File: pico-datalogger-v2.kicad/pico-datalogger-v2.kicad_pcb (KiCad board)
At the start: 2 copper layers, 46 x 60 mm, 35 parts, among them J1 JST-PH2 Bat, J10 Conn_PCB_2, J11 Conn_I2C1, J12 Conn_UART_5V, J13 Conn_I2C1, J14 Conn_I2C0, J2 Conn_Pico_Left, J3 Conn_Pico_Right, J4 Alt-Bat, J5 Conn_LoRa, J6 Conn_Display, J7 Conn_PCB_1, J8 Conn_ADC, J9 Conn_I2C0, Q1 AO3401A, Q2 AO3401A, SW1 SW_ON, SW2 SW_RUN, U1 74LVC2G74, U2 PCF8523T, U4 XTSD, Y1 Crystal

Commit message: added THT-connectors, finished routing
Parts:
- added J15: PCB_2_THT, Connector_PinHeader_2.54mm:PinHeader_1x08_P2.54mm_Vertical, F.Cu at (99.2, 119.7)
- added J16: LoRa_THT, Connector_PinHeader_2.54mm:PinHeader_1x08_P2.54mm_Vertical, F.Cu at (99.2, 147.4)
- added J17: Disp_THT, Connector_PinHeader_2.54mm:PinHeader_1x08_P2.54mm_Vertical, F.Cu at (137.1, 147.4)
- added R5: 10K, Resistor_SMD:R_0402_1005Metric, F.Cu at (128.3, 147.1)
- added R6: 100K, Resistor_SMD:R_0402_1005Metric, F.Cu at (128.4, 149.6)
- added R7: 10K, Resistor_SMD:R_0402_1005Metric, F.Cu at (123.1, 129.8)
- J4: value Alt-Bat -> PCB_1_THT; footprint Connector_PinHeader_2.54mm:PinHeader_1x02_P2.54mm_Vertical -> Connector_PinHeader_2.54mm:PinHeader_1x04_P2.54mm_Vertical; moved to F.Cu
- J7: footprint Connector_JST:JST_SUR_BM04B-SURS-TF_1x04-1MP_P0.80mm_Vertical -> Connector_JST:JST_SUR_BM08B-SURS-TF_1x08-1MP_P0.80mm_Vertical
- SW2: value SW_RUN -> SW_RST
- moved J4 36.5 mm to (108.2, 161.8), turned to 90 degrees
- moved J1 35.2 mm to (141.1, 110.8)
- moved J5 16.6 mm to (92.3, 156.2)
- moved J6 16.1 mm to (142.9, 156.2)
- moved H3 14.1 mm to (93.0, 167.0)
- moved SW1 11.3 mm to (127.5, 165.8)
- moved J7 11.3 mm to (112.0, 167.8)
- moved SW2 11.3 mm to (119.4, 165.8)
- moved H1 10.0 mm to (93.0, 103.0)
- moved H4 10.0 mm to (143.0, 167.0)
- moved J10 10.0 mm to (92.3, 131.5)
- moved J12 10.0 mm to (94.3, 120.9)
- moved BT1 3.60 mm to (136.8, 129.6)
- moved R2 0.85 mm to (122.0, 119.0), turned to -90 degrees
- moved C3 0.25 mm to (121.0, 143.4)
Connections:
- J4 pad 1: +BATT -> GND
- J4 pad 2: GND -> +3V3
- J7 pad 2: +3V3 -> GND
- J7 pad 3: /RUN -> +3V3
- J7 pad 4: /~{ON} -> +3V3
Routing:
- net +3V3: track 134.1 -> 223.5 mm
- net +BATT: track 66.7 -> 32.1 mm
- net /Display_CS: track 4.05 -> 32.5 mm, vias 0 -> 1
- net /SCLK0: track 23.1 -> 47.0 mm
- net /Lora_CS: track 7.16 -> 27.6 mm
- net /Lora_RST: track 7.88 -> 27.7 mm
- net /MISO1: track 16.9 -> 36.3 mm, vias 1 -> 0
- net /Display_RST: track 15.9 -> 35.3 mm, vias 0 -> 1
- net /MOSI1: track 8.60 -> 27.7 mm
- net /Display_DC: track 11.2 -> 30.1 mm
- net /SCLK1: track 10.3 -> 28.4 mm
- net /SDA: track 61.0 -> 79.1 mm
- net /MOSI0: track 27.0 -> 43.5 mm, vias 0 -> 2
- net /RUN: track 47.8 -> 63.6 mm
- net /Display_BUSY: track 27.5 -> 40.6 mm, vias 0 -> 1
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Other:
- board size 46 x 60 mm -> 56 x 70 mm
- board text added: "CS"
- board text added: "RST"
- board text removed: "RUN"

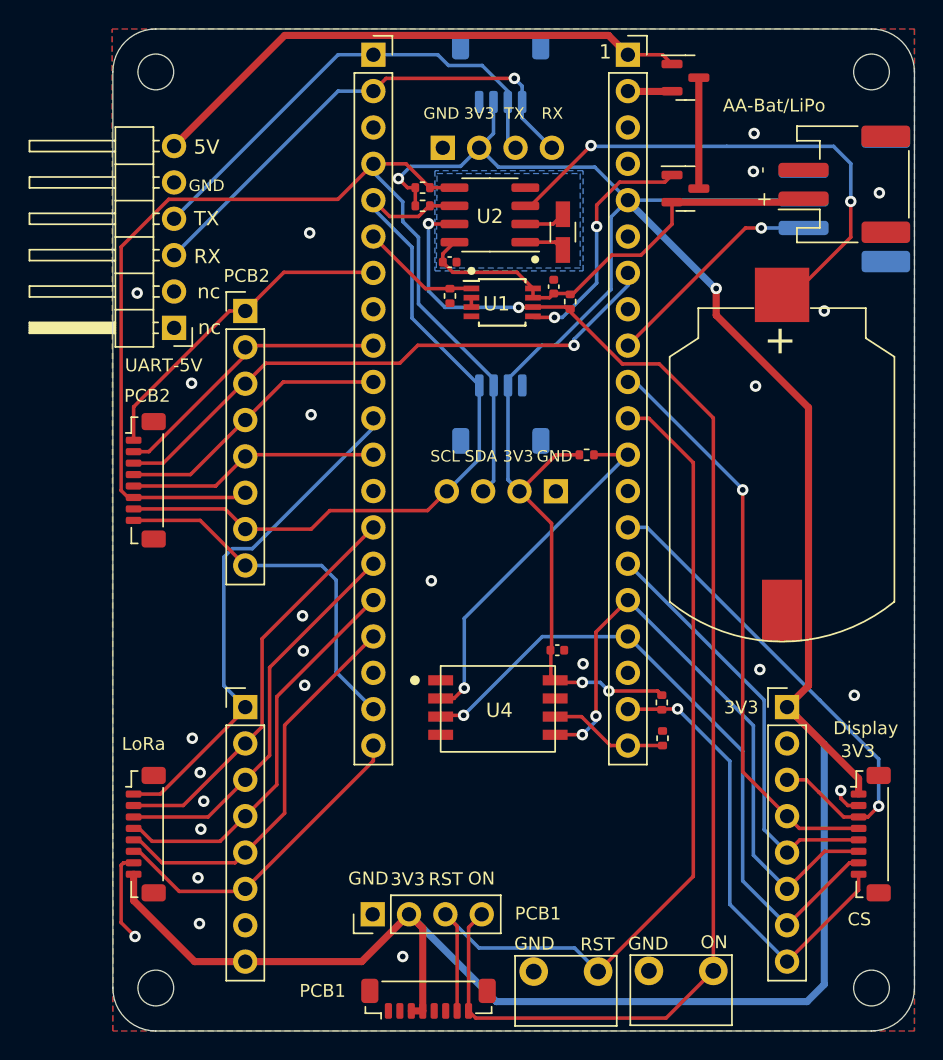
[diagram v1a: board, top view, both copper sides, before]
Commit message: Datalogger-v2 Rev 1.95: larger PCB-size, THT-connectors
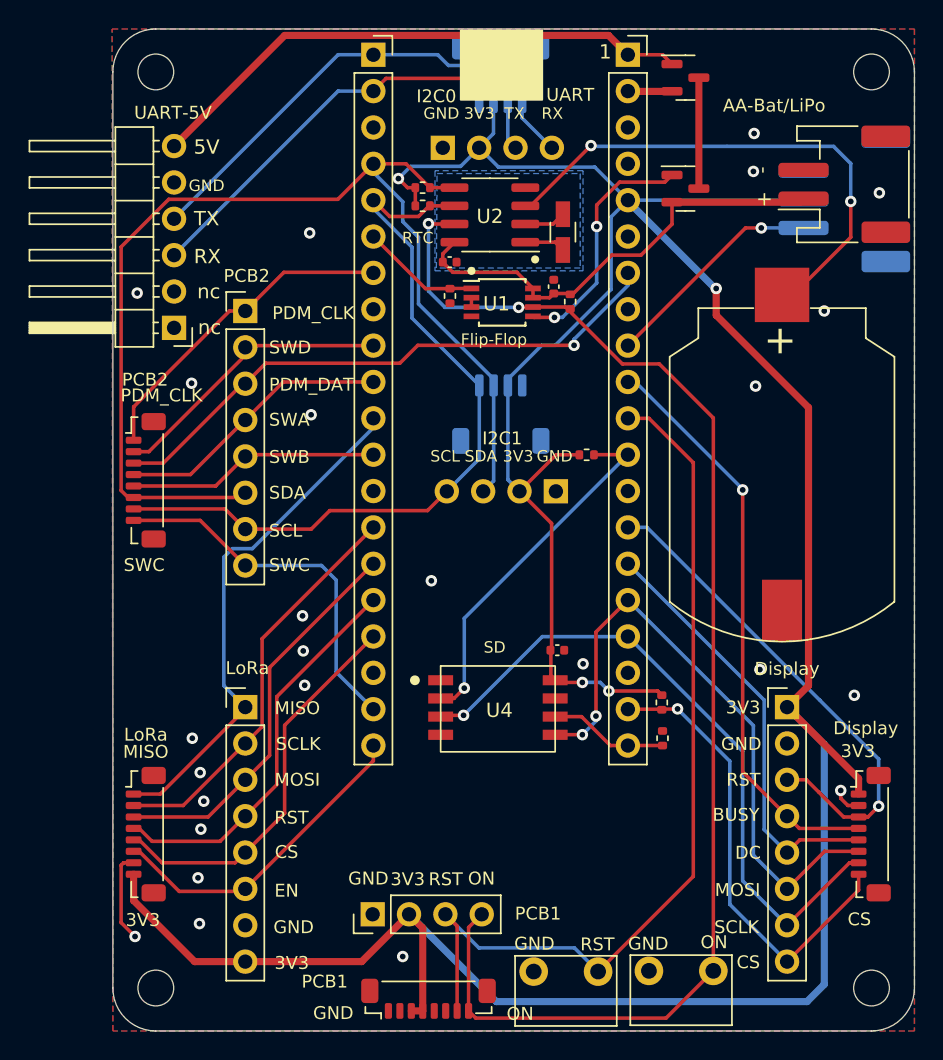
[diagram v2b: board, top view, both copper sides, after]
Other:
- board text added: "BUSY"
- board text added: "DC"
- board text added: "EN"
- board text added: "Flip-Flop"
- board text added: "I2C0"
- board text added: "MISO"
- board text added: "MOSI"
- board text added: "PDM_CLK"
- board text added: "PDM_DAT"
- board text added: "RTC"
- board text added: "SCLK"
- board text added: "SD"
- board text added: "SWA"
- board text added: "SWB"
- board text added: "SWC"
- board text added: "SWD"
- board text added: "UART"
- board text added: "https://github.com/bablokb/pcb-pico-datalogger https://opendeved.net/ilce Rev 1.95"
- board text removed: "https://github.com/bablokb/pcb-pico-datalogger https://opendeved.net/ilce Rev 0.94"

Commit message: Datalogger-v2 Rev 2.00: larger PCB-size, THT-connectors (ready for prod)
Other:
- board text added: "https://github.com/bablokb/pcb-pico-datalogger https://opendeved.net/ilce Rev 2.00"
- board text removed: "https://github.com/bablokb/pcb-pico-datalogger https://opendeved.net/ilce Rev 1.95"
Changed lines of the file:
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@@
     (property "Sheetname" "")
     (property "exclude_from_bom" "")
-    (attr through_hole exclude_from_bom)
+    (attr through_hole exclude_from_pos_files exclude_from_bom)
     (fp_text reference "J4" (at 0 -2.33 90) (layer "F.SilkS") hide
       (effects (font (size 1 1) (thickness 0.15)))
@@
     (property "Sheetname" "")
     (property "exclude_from_bom" "")
-    (attr through_hole exclude_from_bom)
+    (attr through_hole exclude_from_pos_files exclude_from_bom)
     (fp_text reference "J16" (at 0 -2.33) (layer "F.SilkS") hide
       (effects (font (size 1 1) (thickness 0.15)))
@@
     (property "Sheetname" "")
     (property "exclude_from_bom" "")
-    (attr through_hole exclude_from_bom)
+    (attr through_hole exclude_from_pos_files exclude_from_bom)
     (fp_text reference "J15" (at 0 -2.33) (layer "F.SilkS") hide
       (effects (font (size 1 1) (thickness 0.15)))
@@
     (pad "8" smd roundrect (at 2.8 0.85) (size 0.5 1.1) (layers "F.Cu" "F.Paste" "F.Mask") (roundrect_rratio 0.25)
       (net 39 "/~{ON}") (pinfunction "Pin_8") (pintype "passive"))
-    (pad "MP" smd roundrect (at -4.1 -0.55) (size 1.2 1.7) (layers "F.Cu" "F.Paste" "F.Mask") (roundrect_rratio 0.208333))
-    (pad "MP" smd roundrect (at 4.1 -0.55) (size 1.2 1.7) (layers "F.Cu" "F.Paste" "F.Mask") (roundrect_rratio 0.208333))
+    (pad "MP" smd roundrect (at -4.1 -0.55) (size 1.2 1.7) (layers "F.Cu" "F.Paste" "F.Mask") (roundrect_rratio 0.2083333333))
+    (pad "MP" smd roundrect (at 4.1 -0.55) (size 1.2 1.7) (layers "F.Cu" "F.Paste" "F.Mask") (roundrect_rratio 0.2083333333))
     (model "${KICAD6_3DMODEL_DIR}/Connector_JST.3dshapes/JST_SUR_BM08B-SURS-TF_1x08-1MP_P0.80mm_Vertical.wrl"
       (offset (xyz 0 0 0))
@@
     (property "Sheetname" "")
     (property "exclude_from_bom" "")
-    (attr through_hole exclude_from_bom)
+    (attr through_hole exclude_from_pos_files exclude_from_bom)
     (fp_text reference "J17" (at 0 -2.33) (layer "F.SilkS") hide
       (effects (font (size 1 1) (thickness 0.15)))
@@
     (property "Sheetfile" "pico-datalogger-v2.kicad_sch")
     (property "Sheetname" "")
-    (attr through_hole exclude_from_pos_files)
+    (property "exclude_from_bom" "")
+    (attr through_hole exclude_from_pos_files exclude_from_bom)
     (fp_text reference "SW1" (at -1.4 -3.6 90) (layer "F.SilkS") hide
       (effects (font (size 1 1) (thickness 0.15)))
@@
     (property "Sheetfile" "pico-datalogger-v2.kicad_sch")
     (property "Sheetname" "")
-    (attr through_hole exclude_from_pos_files)
+    (property "exclude_from_bom" "")
+    (attr through_hole exclude_from_pos_files exclude_from_bom)
     (fp_text reference "SW2" (at -1.25 -2.5 90) (layer "F.SilkS") hide
       (effects (font (size 1 1) (thickness 0.15)))
@@
     (effects (font (size 0.9 0.9) (thickness 0.15)) (justify mirror))
   )
-  (gr_text "https://github.com/bablokb/pcb-pico-datalogger\nhttps://opendeved.net/ilce               Rev 1.95" (at 93.35 123.75 90) (layer "B.SilkS")
+  (gr_text "https://github.com/bablokb/pcb-pico-datalogger\nhttps://opendeved.net/ilce               Rev 2.00" (at 93.35 123.75 90) (layer "B.SilkS")
     (effects (font (size 1 1) (thickness 0.15)) (justify left mirror))
   )

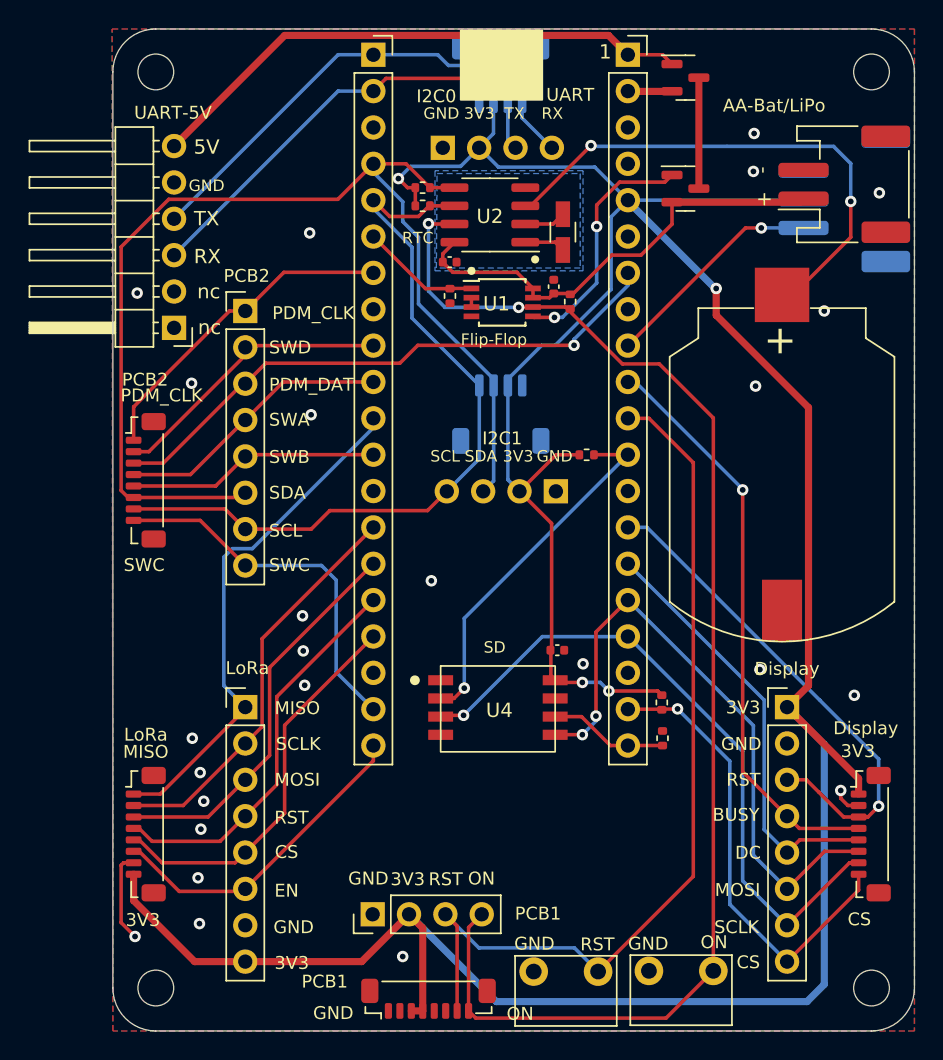
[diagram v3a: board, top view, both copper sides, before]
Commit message: Datalogger-v2 Rev 2.01: rotated display connector (ready for prod)
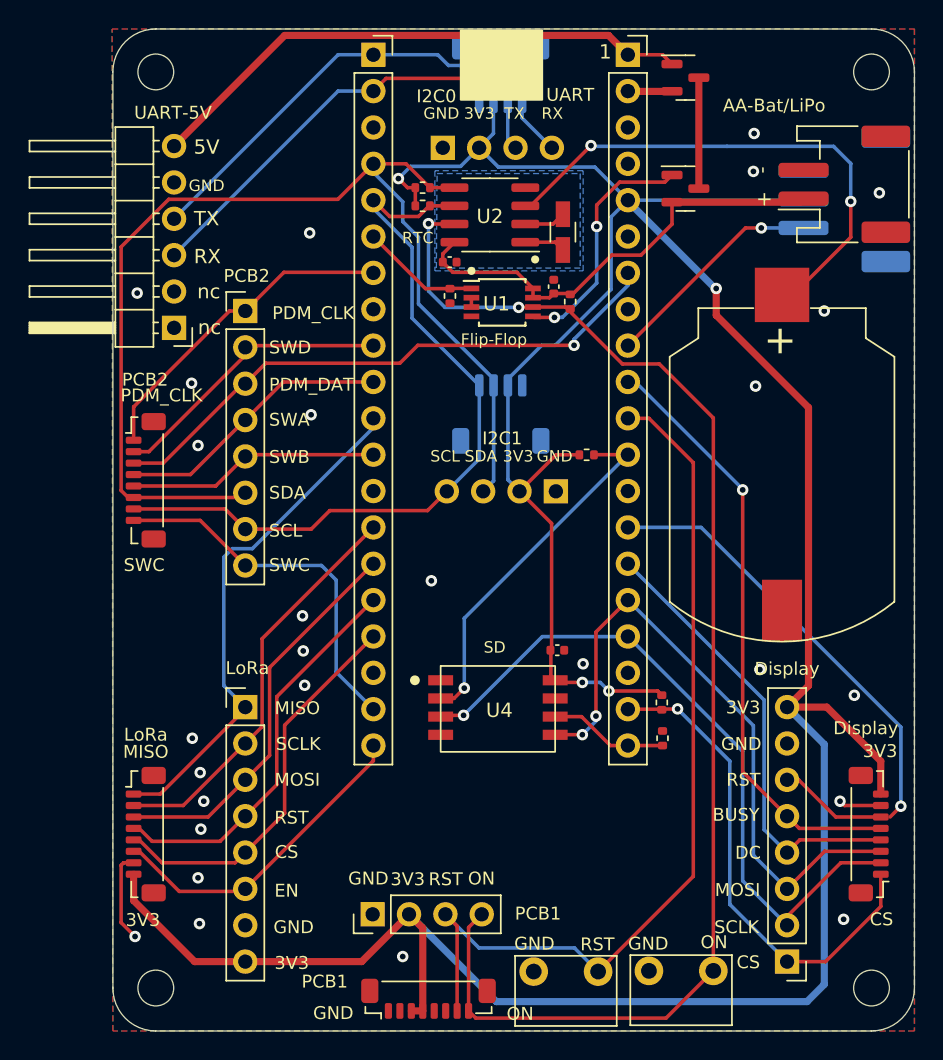
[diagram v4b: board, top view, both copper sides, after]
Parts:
- moved J17 17.8 mm to (137.1, 165.2), turned to 180 degrees
- moved J6 0.15 mm to (142.8, 156.2), turned to 90 degrees
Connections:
- J17 pad 1: +3V3 -> /Display_CS
- J17 pad 2: GND -> /SCLK0
- J17 pad 3: /Display_RST -> /MOSI0
- J17 pad 4: /Display_BUSY -> /Display_DC
- J17 pad 5: /Display_DC -> /Display_BUSY
- J17 pad 6: /MOSI0 -> /Display_RST
- J17 pad 7: /SCLK0 -> GND
- J17 pad 8: /Display_CS -> +3V3
- J6 pad 1: +3V3 -> /Display_CS
- J6 pad 2: GND -> /SCLK0
- J6 pad 3: /Display_RST -> /MOSI0
- J6 pad 4: /Display_BUSY -> /Display_DC
- J6 pad 5: /Display_DC -> /Display_BUSY
- J6 pad 6: /MOSI0 -> /Display_RST
- J6 pad 7: /SCLK0 -> GND
- J6 pad 8: /Display_CS -> +3V3
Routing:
- net /Display_RST: track 35.3 -> 39.1 mm
- net +3V3: track 223.5 -> 225.7 mm
- net /Display_CS: track 32.5 -> 34.7 mm
- net /SCLK0: track 47.0 -> 48.9 mm
- net /MOSI0: track 43.5 -> 45.0 mm
- net /Display_DC: track 30.1 -> 31.7 mm
- net /Display_BUSY: track 40.6 -> 42.2 mm
- net GND: track 8.33 -> 9.30 mm, vias 25 -> 27
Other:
- board text added: "https://github.com/bablokb/pcb-pico-datalogger https://opendeved.net/ilce Rev 2.01"
- board text removed: "https://github.com/bablokb/pcb-pico-datalogger https://opendeved.net/ilce Rev 2.00"

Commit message: Datalogger-v2 Rev 2.10: Stemma/Qt on top (ready for prod)
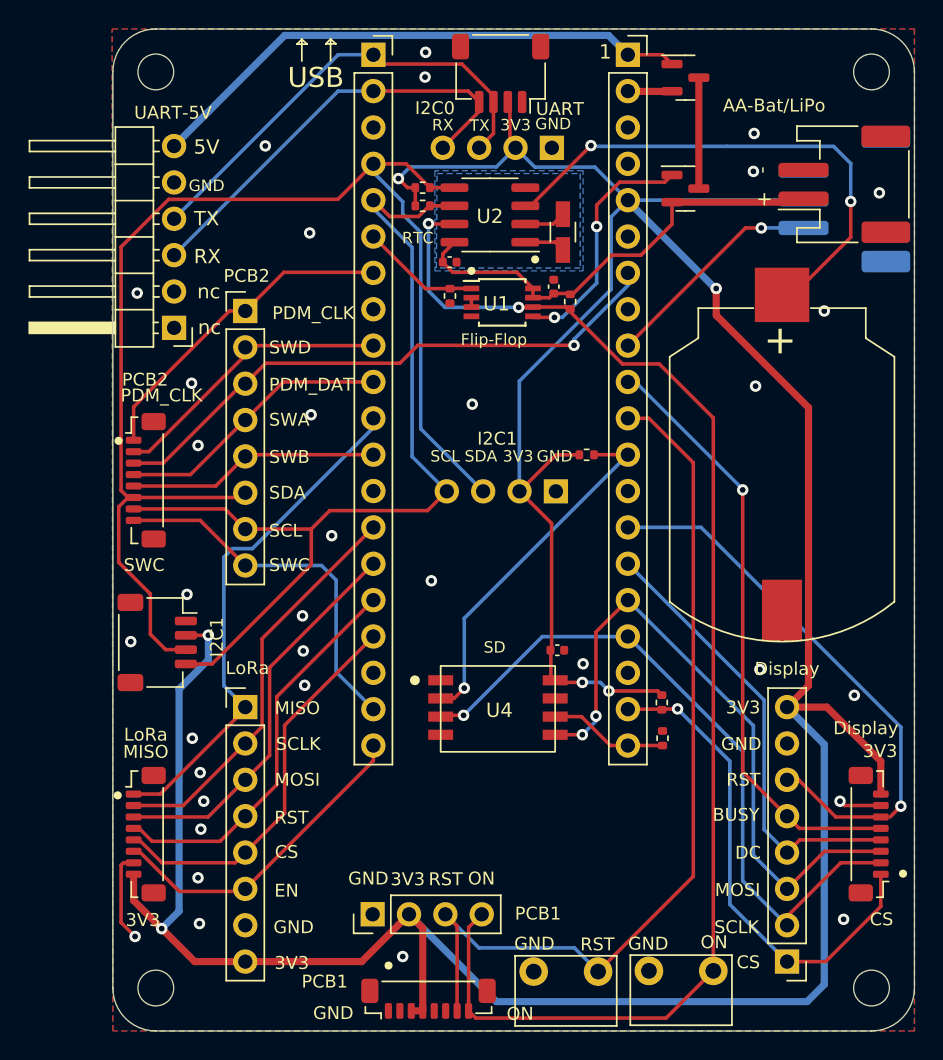
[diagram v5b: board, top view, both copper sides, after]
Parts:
- J11, J9: moved to F.Cu
- J13: value Conn_I2C1 -> THT_I2C1
- J14: value Conn_I2C0 -> THT_I2C0
- moved J11 28.8 mm to (93.1, 142.9), turned to -90 degrees
- moved J14 7.62 mm to (120.7, 108.3), turned to 90 degrees
- turned J9 to 180 degrees
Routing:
- net +3V3: track 225.7 -> 247.6 mm, vias 4 -> 6
- net /SDA: track 79.1 -> 92.1 mm
- net /SCL: track 54.3 -> 66.6 mm
- net /RX: track 35.0 -> 30.6 mm, vias 1 -> 0
- net GND: vias 27 -> 34
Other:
- board text added: "USB"
- board text added: "https://github.com/bablokb/pcb-pico-datalogger https://opendeved.net/ilce Rev 2.10"
- board text removed: "I2C0/UART-3V3"
- board text removed: "https://github.com/bablokb/pcb-pico-datalogger https://opendeved.net/ilce Rev 2.01"
